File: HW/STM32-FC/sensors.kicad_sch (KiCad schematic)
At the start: 13 parts, among them U5 BMP280, U7 BMI088, U8 LIS2MDLTR

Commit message: 250102:STM32F407VET
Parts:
- added C27, C29: 10uF, Capacitor_SMD:C_0402_1005Metric, symbol Device:C_Small
- added C28: 100nF, Capacitor_SMD:C_0402_1005Metric, symbol Device:C_Small
- added D2: B5819W, Diode_SMD:D_SOD-123, symbol Device:D_Schottky_Small
- added J3: Molex 53048-03, Connector_Molex:Molex_PicoBlade_53048-0310_1x03_P1.25mm_Horizontal, symbol Connector_Generic:Conn_01x03
- added U1: AMS1117-3.3, Package_TO_SOT_SMD:SOT-223-3_TabPin2, symbol Regulator_Linear:AMS1117-3.3
- R9: value 1k -> 10k
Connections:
- net +BATT: now also J3.1 (Pin_1)
- net GND: now also C27.2, C28.2, C29.2, J3.2 (Pin_2), U1.1 (GND)
- net +3.3V renamed +3.3VA
- net +3.3VA: now also C28.1, C29.1, U1.2 (VO)
- new net: D2.2 (A), J3.3 (Pin_3)
- new net +5V: C27.1, D2.1 (K), U1.3 (VI)
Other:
- note added: "Voltage Regulator"

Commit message: Big Update:IMU/RC/Conn./MCU
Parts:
- removed C17, C18: 100nF, Capacitor_SMD:C_0603_1608Metric_Pad1.08x0.95mm_HandSolder, symbol Device:C_Small
- removed C27, C29: 10uF, Capacitor_SMD:C_0402_1005Metric, symbol Device:C_Small
- removed C28: 100nF, Capacitor_SMD:C_0402_1005Metric, symbol Device:C_Small
- removed D2: B5819W, Diode_SMD:D_SOD-123, symbol Device:D_Schottky_Small
- removed U1: AMS1117-3.3, Package_TO_SOT_SMD:SOT-223-3_TabPin2, symbol Regulator_Linear:AMS1117-3.3
- removed U5: BMP280, Package_LGA:Bosch_LGA-8_2x2.5mm_P0.65mm_ClockwisePinNumbering, symbol Sensor_Pressure:BMP280
- removed U7: BMI088, Custom_Parts:PQFN50P450X300X100-16N, symbol BMI088:BMI088
- added C20: 100nF, Capacitor_SMD:C_0402_1005Metric, symbol Device:C_Small
- added C23: 2.2nF, Capacitor_SMD:C_0402_1005Metric, symbol Device:C_Small
- added C24: 10nF, Capacitor_SMD:C_0402_1005Metric, symbol Device:C_Small
- added C25, C26: 100nF, Capacitor_SMD:C_0603_1608Metric_Pad1.08x0.95mm_HandSolder, symbol Device:C_Small
- added U6: BMI323, BMI323_BOS, symbol BMI323:BMI323
- added U7: ICM-42688-P, ICM-42688-P:PQFN50P300X250X97-14N, symbol ICM-42688-P:ICM-42688-P
- added U8: BMP280, Package_LGA:Bosch_LGA-8_2x2.5mm_P0.65mm_ClockwisePinNumbering, symbol Sensor_Pressure:BMP280
- C21: value 100nF -> 0.1nF
- J4: renamed from J3; value Molex 53048-03 -> BATT; footprint Connector_Molex:Molex_PicoBlade_53048-0310_1x03_P1.25mm_Horizontal -> Connector_JST:JST_ZH_B2B-ZR_1x02_P1.50mm_Vertical; symbol Connector_Generic:Conn_01x03 -> Connector_Generic:Conn_01x02; now in the parts list
- renumbered C23 to C27, C24 to C28, C25 to C29, C26 to C30, R9 to R10, R10 to R11, U8 to U9
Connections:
- net BARO_NSS: now also U8.2 (CSB)
- net GND: now also C22.1, C20.2, C23.2, C24.2, C25.2, C26.2, U6.6 (GNDIO), U6.7 (GND), U7.6 (GND), U8.1 (GND), U8.7 (GND); no longer C22.2
- net SS_SPI_MISO: now also U7.1 (AP_SDO/AP_AD0), U8.5 (SDO); no longer U9.7 (INT/DRDY/SDO)
- net SS_SPI_MOSI: now also U7.14 (AP_SDA/AP_SDIO/AP_SDI), U8.3 (SDI); no longer U9.4 (SDA/SDI/SDO)
- net SS_SPI_SCK: now also U7.13 (AP_SCL/AP_SCLK), U8.4 (SCK); no longer U9.1 (SCL/SPC)
- net +3.3VA renamed +3.3V
- net +3.3V: now also C22.2, C20.1, C23.1, C24.1, C25.1, C26.1, U6.5 (VDDIO), U6.8 (VDD), U7.5 (VDDIO), U7.8 (VDD), U8.6 (VDDIO), U8.8 (VDD); no longer C22.1
- new net GYRO1_NSS: U7.12 (AP_CS)
- new net GYRO2_NSS: U6.12 (CSB)
- new net SS2_SPI_MISO: U6.1 (SDO), U9.7 (INT/DRDY/SDO)
- new net SS2_SPI_MOSI: U6.14 (SDX), U9.4 (SDA/SDI/SDO)
- new net SS2_SPI_SCK: U6.13 (SCX), U9.1 (SCL/SPC)
- no-connect marks 4 -> 9
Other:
- note added: "Accelerometer/Gyroscope1"
- note added: "Accelerometer/Gyroscope2"
- note added: "JST ZH 1.5mm 2P PC1 : ADC123_IN11"
- note removed: "Accelerometer/Gyroscope"
- note removed: "PC4 : ADC12_IN14"
- note removed: "Voltage Regulator"
- company: casterian.net -> INHA UNIV. NARAE
- title: STM32 Flight Controller -> Sensors
- moved on the sheet: C27, C28, C29, C30, R10, R11, U9

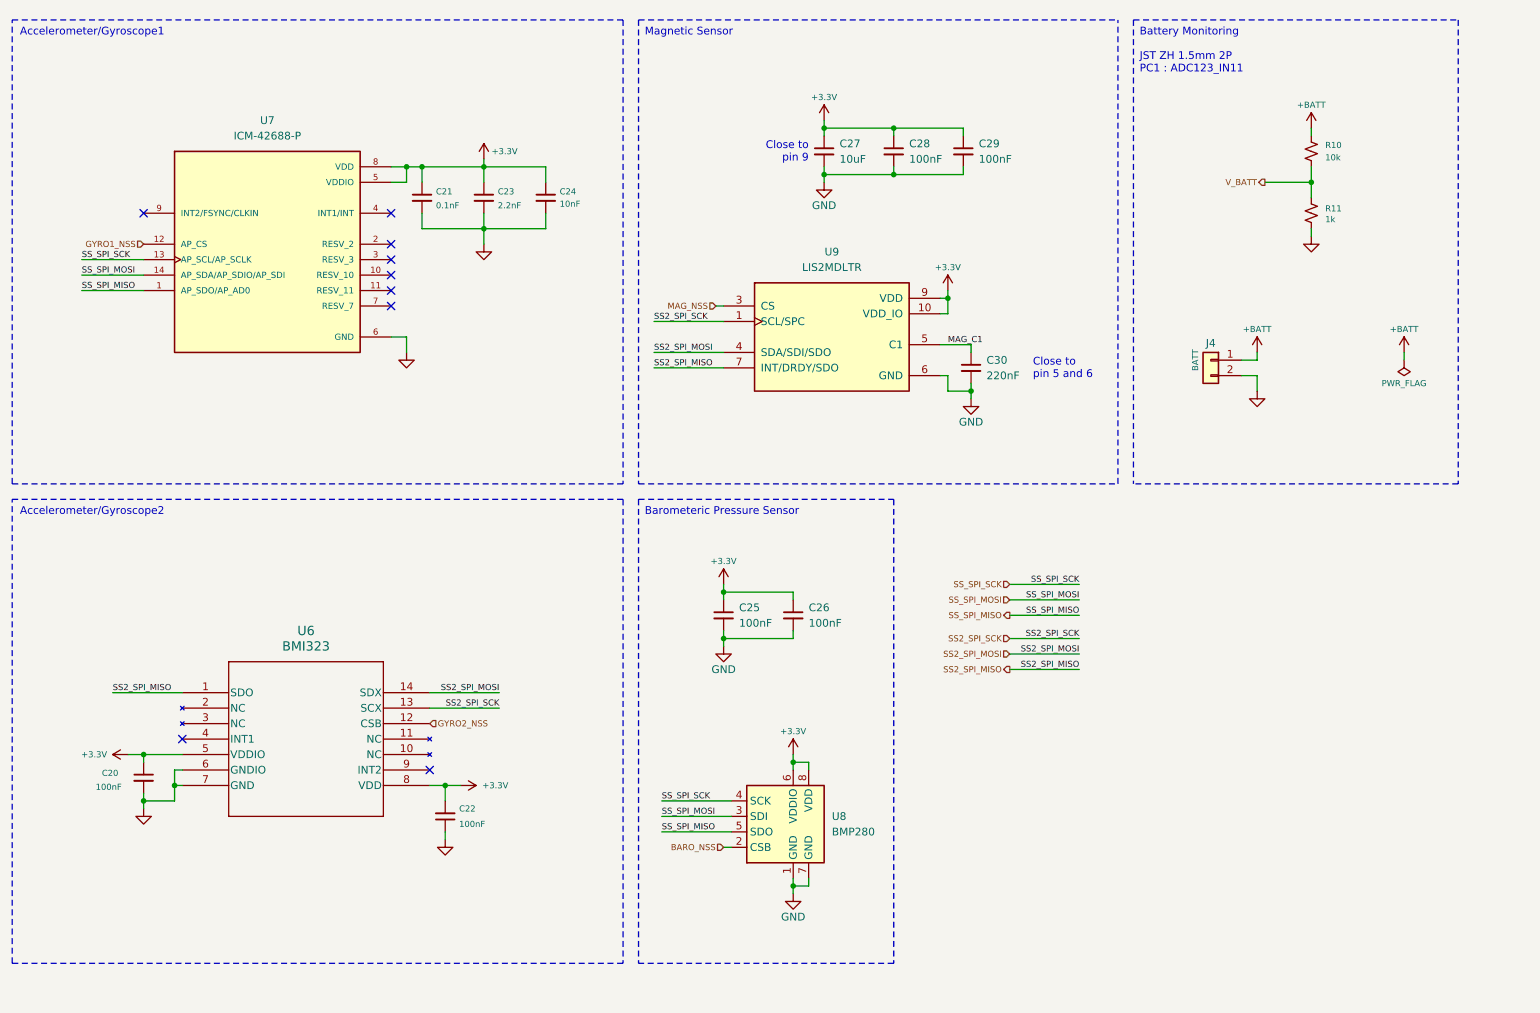
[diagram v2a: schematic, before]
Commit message: 2025.01.03v2:PM(Power Module) added
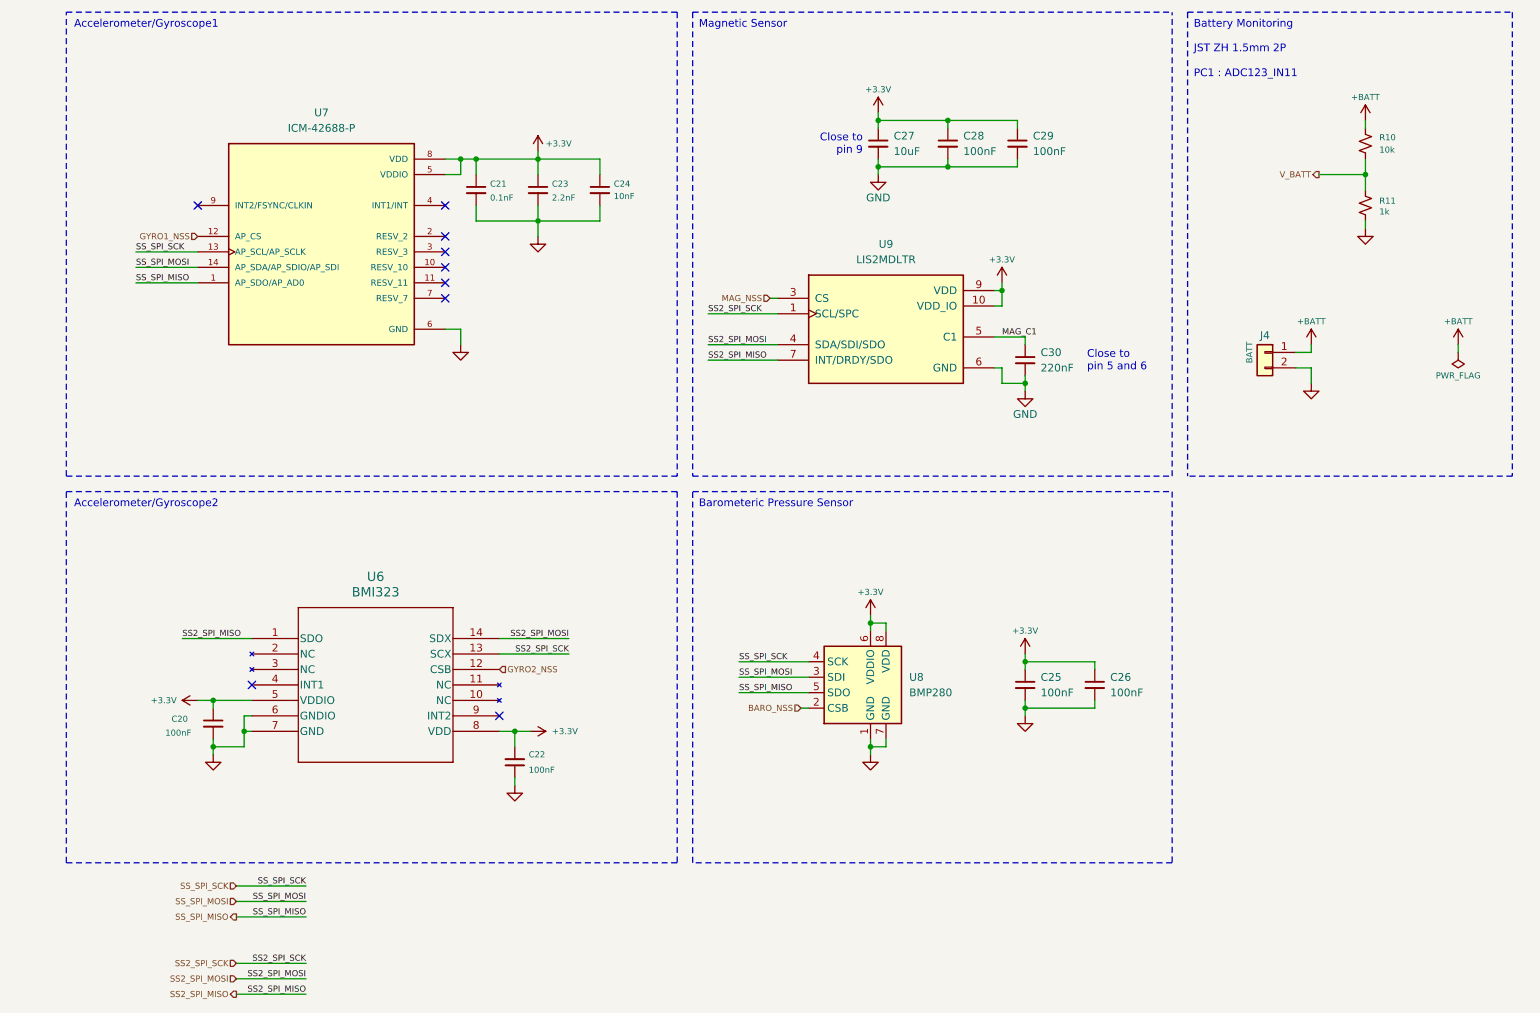
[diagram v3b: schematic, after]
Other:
- company: INHA UNIV. NARAE -> NARAE
- moved on the sheet: C20, C21, C22, C23, C24, C25, C26, C27, C28, C29, C30, J4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

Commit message: Baro/SD Card update
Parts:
- removed C25, C26: 100nF, Capacitor_SMD:C_0603_1608Metric_Pad1.08x0.95mm_HandSolder, symbol Device:C_Small
- removed U7: ICM-42688-P, ICM-42688-P:PQFN50P300X250X97-14N, symbol ICM-42688-P:ICM-42688-P
- removed U8: BMP280, Package_LGA:Bosch_LGA-8_2x2.5mm_P0.65mm_ClockwisePinNumbering, symbol Sensor_Pressure:BMP280
- added C26: 4.7u, Capacitor_SMD:C_0402_1005Metric, symbol Device:C
- added R15: 10k, Resistor_SMD:R_0402_1005Metric, symbol Device:R_Small_US
- added U7: ICM-42688-P, ICM-42688-P:IIM42352_HandSolder, symbol ICM-42688-P:ICM-42688-P_COMPACT
- added U9: LPS22HH, Package_LGA:ST_HLGA-10_2x2mm_P0.5mm_LayoutBorder3x2y, symbol Sensor_Pressure:LPS22HH
- J7: renamed from J4; value BATT -> JST ZH 1.5mm 2P; footprint Connector_JST:JST_ZH_B2B-ZR_1x02_P1.50mm_Vertical -> Connector_JST:JST_ZH_S2B-ZR-SM4A-TF_1x02-1MP_P1.50mm_Horizontal
- U6: footprint BMI323_BOS -> BMI323:BMI323_HandSolder
- U8: renamed from U9; footprint Custom_Parts:PQFN50P200X200X70-12N -> LIS2MDLTR:LIS2MDLTR_HandSolder
- renumbered C20 to C21, C21 to C22, C22 to C23, C23 to C24, C24 to C25, R10 to R16, R11 to R17
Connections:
- net +3.3V: now also C26.2, R15.1, U7.5 (VDDIO), U7.8 (VDD), U9.1 (Vdd_IO), U9.10 (VDD)
- net BARO_NSS: now also R15.2, U9.6 (~{CS})
- net GND: now also C26.1, U7.6 (GND), U9.3 (GND), U9.8 (GND), U9.9 (GND)
- net GYRO1_NSS: now also U7.12 (AP_CS)
- net SS_SPI_MISO: now also U7.1 (AP_SDO/AP_AD0), U9.5 (SA0)
- net SS_SPI_MOSI: now also U7.14 (AP_SDA/AP_SDIO/AP_SDI), U9.4 (SDA)
- net SS_SPI_SCK: now also U7.13 (AP_SCL/AP_SCLK), U9.2 (SCL)
- new net BARO_INT: U9.7 (INT_DRDY)

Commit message: 2025.01.16
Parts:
- U7: renamed from U8; footprint LIS2MDLTR:LIS2MDLTR_HandSolder -> LIS2MDLTR:LIS2MDLTR
- renumbered C27 to C21, C28 to C22, C29 to C23, C22 to C24, C24 to C25, C25 to C26, C30 to C27, C26 to C28, C21 to C29, C23 to C30, R16 to R15, R17 to R16, R15 to R17, U7 to U6, U6 to U8

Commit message: 2025.01.17 : PCB layout
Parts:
- J5: renamed from J7; footprint Connector_JST:JST_ZH_S2B-ZR-SM4A-TF_1x02-1MP_P1.50mm_Horizontal -> JST_ZH:JST_ZH_S2B-ZR-SM4A-TF_1x02-1MP_P1.50mm_Horizontal
- U6: renamed from U8; footprint BMI323:BMI323_HandSolder -> BMI323:BMI323_L
- U7: renamed from U6; footprint ICM-42688-P:IIM42352_HandSolder -> ICM-42688-P:IIM42352_L
- U9: footprint Package_LGA:ST_HLGA-10_2x2mm_P0.5mm_LayoutBorder3x2y -> LPS22HH:ST_HLGA-10_2x2mm_P0.5mm_LayoutBorder3x2y
- renumbered C29 to C21, C24 to C22, C30 to C23, C25 to C24, C26 to C25, C28 to C26, C21 to C27, C22 to C28, C23 to C29, C27 to C30, R17 to R16, R15 to R17, R16 to R18, U7 to U8

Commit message: 2025.02.05 PCB routing 3
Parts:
- R17: value 10k -> 15k
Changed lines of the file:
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@@
 			)
 		)
-		(property "Value" "10k"
+		(property "Value" "15k"
 			(at 238.506 35.306 0)
 			(effects
